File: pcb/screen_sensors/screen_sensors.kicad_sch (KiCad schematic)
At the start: 14 parts, among them J1 WAVESHARE_I2C, J2 BOILER_PROBE, J3 XDB401_ANALOG, U1 ADS1115IDGSR, U2 SHT40-AD1B

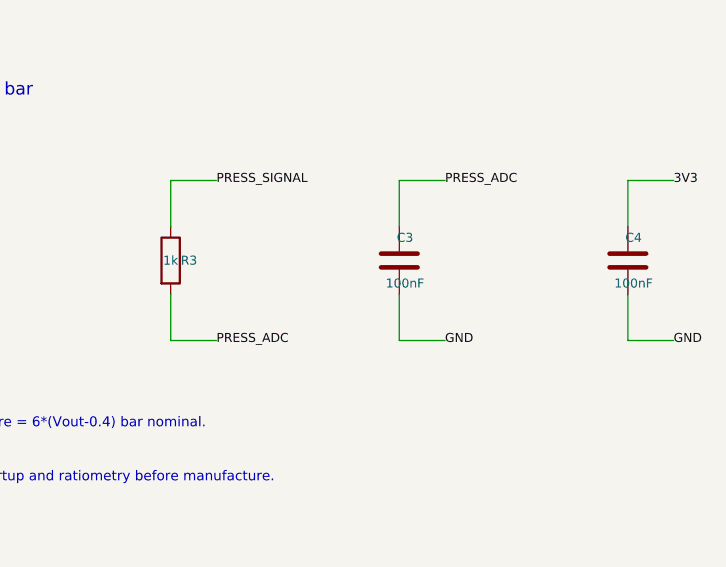
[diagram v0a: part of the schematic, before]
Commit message: Lower the screen sensors pressure filter to 16 Hz with a 10 µF C3
The 1 kΩ / 100 nF filter only removed fast edges, letting 50/100 Hz mains
pickup alias into the ADS1115 samples once the sensor cable ran near the
230 V wiring. The design notes now record the measured sensor behaviour and
leave the 3.3 V or 5 V supply choice open.

Co-Authored-By: Claude Opus 5.5 <noreply@anthropic.com>
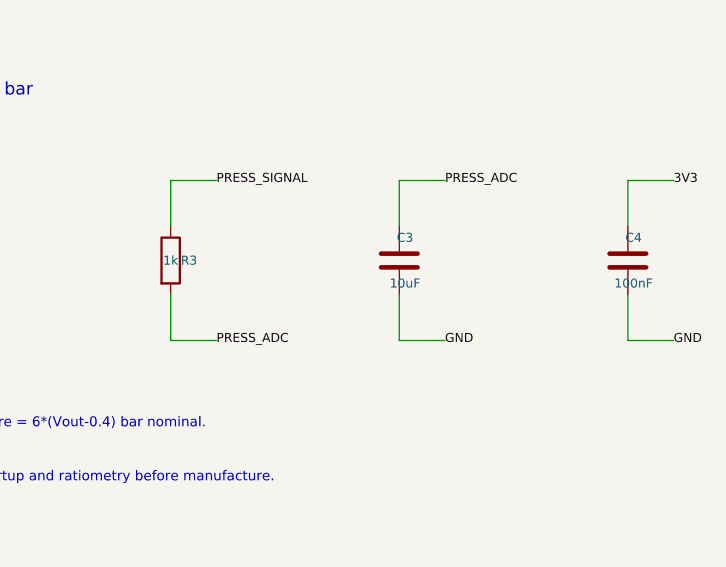
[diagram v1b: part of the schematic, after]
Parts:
- C3: value 100nF -> 10uF; LCSC C14663 -> C19702; MPN CC0603KRX7R9BB104 -> CL10A106KP8NNNC; Note Input filter at ADC; 1k/100nF fc~1.59kHz -> Input filter at ADC; 1k/10uF fc~16Hz; X5R 10V
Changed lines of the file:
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@@
 (symbol (lib_id "Device:C") (at 233.68 116.84 0) (unit 1) (in_bom yes) (on_board yes) (dnp no)
 (property "Reference" "C3" (at 234.315 114.3 0) (effects (font (size 1.0 1.0)) ))
-(property "Value" "100nF" (at 234.315 119.38000000000001 0) (effects (font (size 1.0 1.0)) ))
+(property "Value" "10uF" (at 234.315 119.38000000000001 0) (effects (font (size 1.0 1.0)) ))
 (property "Footprint" "Capacitor_SMD:C_0603_1608Metric" (at 234.64520000000002 120.65 0) (effects (font (size 1.0 1.0)) (hide yes)))
 (property "Datasheet" "" (at 233.68 116.84 0) (effects (font (size 1.0 1.0)) (hide yes)))
-(property "LCSC" "C14663" (at 233.68 124.84 0) (effects (font (size 1.0 1.0)) (hide yes)))
-(property "Note" "Input filter at ADC; 1k/100nF fc~1.59kHz" (at 233.68 124.84 0) (effects (font (size 1.0 1.0)) (hide yes)))
-(property "MPN" "CC0603KRX7R9BB104" (at 233.68 124.84 0) (effects (font (size 1.0 1.0)) (hide yes)))
+(property "LCSC" "C19702" (at 233.68 124.84 0) (effects (font (size 1.0 1.0)) (hide yes)))
+(property "Note" "Input filter at ADC; 1k/10uF fc~16Hz; X5R 10V" (at 233.68 124.84 0) (effects (font (size 1.0 1.0)) (hide yes)))
+(property "MPN" "CL10A106KP8NNNC" (at 233.68 124.84 0) (effects (font (size 1.0 1.0)) (hide yes)))
 (pin "1")
 (pin "2")
